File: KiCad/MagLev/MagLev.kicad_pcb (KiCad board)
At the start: 2 copper layers, 79 parts, among them J1 Barrel_Jack, Q1 ZX5T851GTA, Q2 ZX5T1951GTA, Q3 ZX5T851GTA, Q4 ZX5T1951GTA, Q5 ZX5T1951GTA, Q6 ZX5T851GTA, Q7 ZX5T1951GTA, Q8 ZX5T851GTA, Q9 ZX5T1951GTA, U1 LM324, U10 DRV5505, U11 DRV5505, U12 DRV5505, U2 LM324, U3 L78L05_SO8, U4 TL431A, U5 LM393

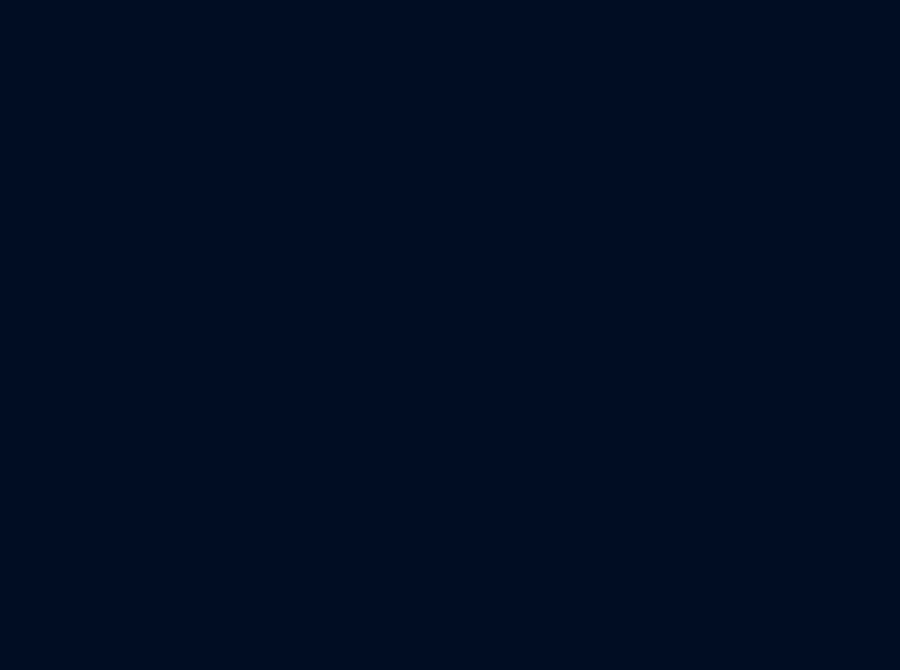
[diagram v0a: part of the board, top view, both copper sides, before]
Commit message: Update spice model to match enbs design. Add TVS diodes to schematic.
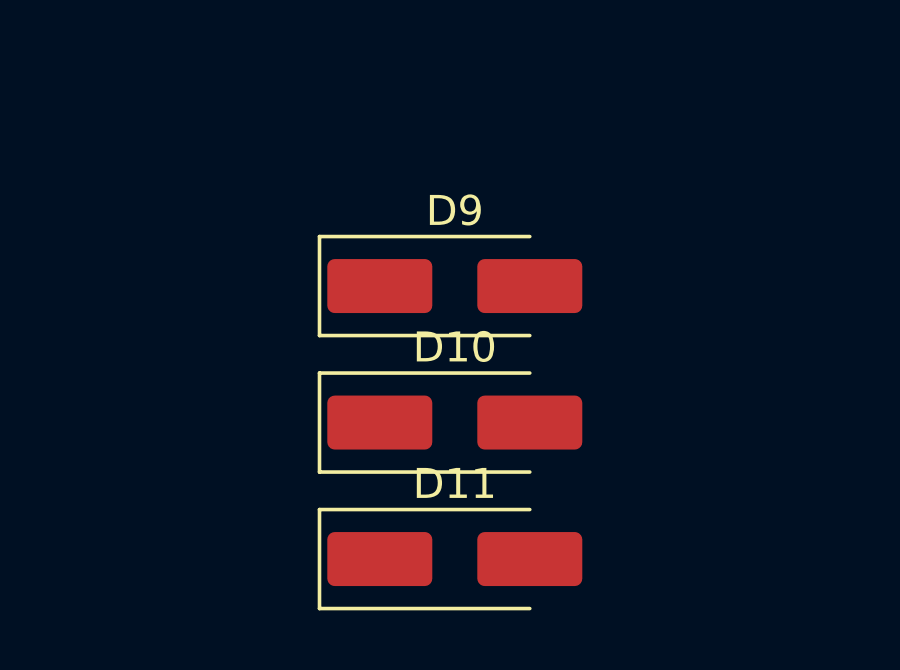
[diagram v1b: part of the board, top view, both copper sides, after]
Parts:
- added D10: SMAJ12A, Diode_SMD:D_SMA_Handsoldering, F.Cu at (-38.1, 145.3)
- added D11: SMAJ12A, Diode_SMD:D_SMA_Handsoldering, F.Cu at (-38.1, 149.9)
- added D9: SMAJ5.0A, Diode_SMD:D_SMA_Handsoldering, F.Cu at (-38.1, 140.8)
- renumbered L1 to X1, L2 to X2, L3 to Y1, L4 to Y2

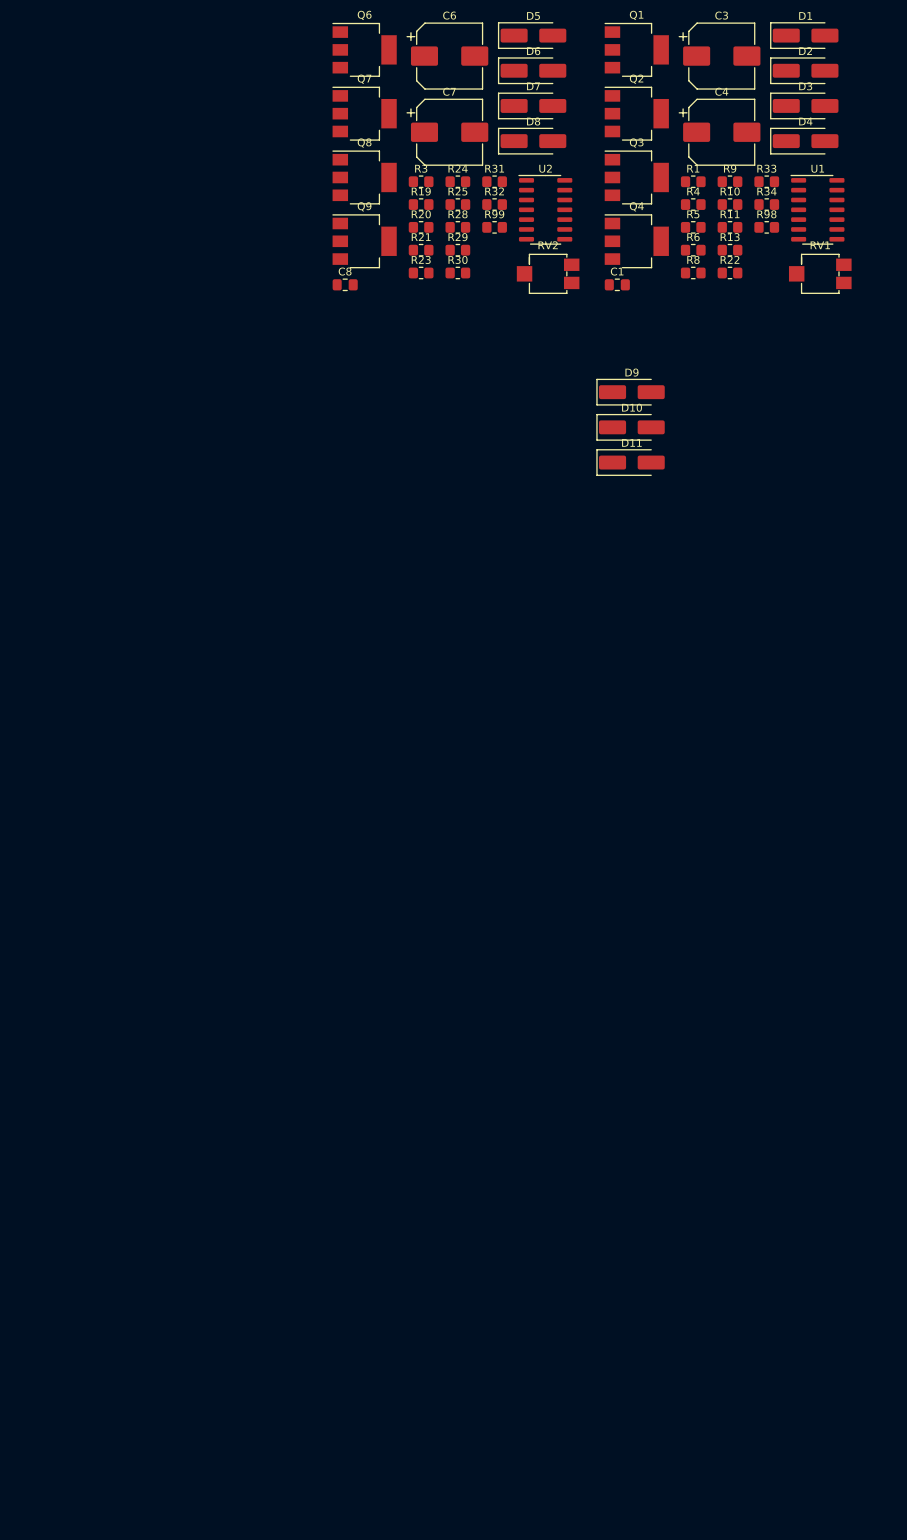
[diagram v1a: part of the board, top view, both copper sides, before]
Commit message: Assign footprints to MCU components.
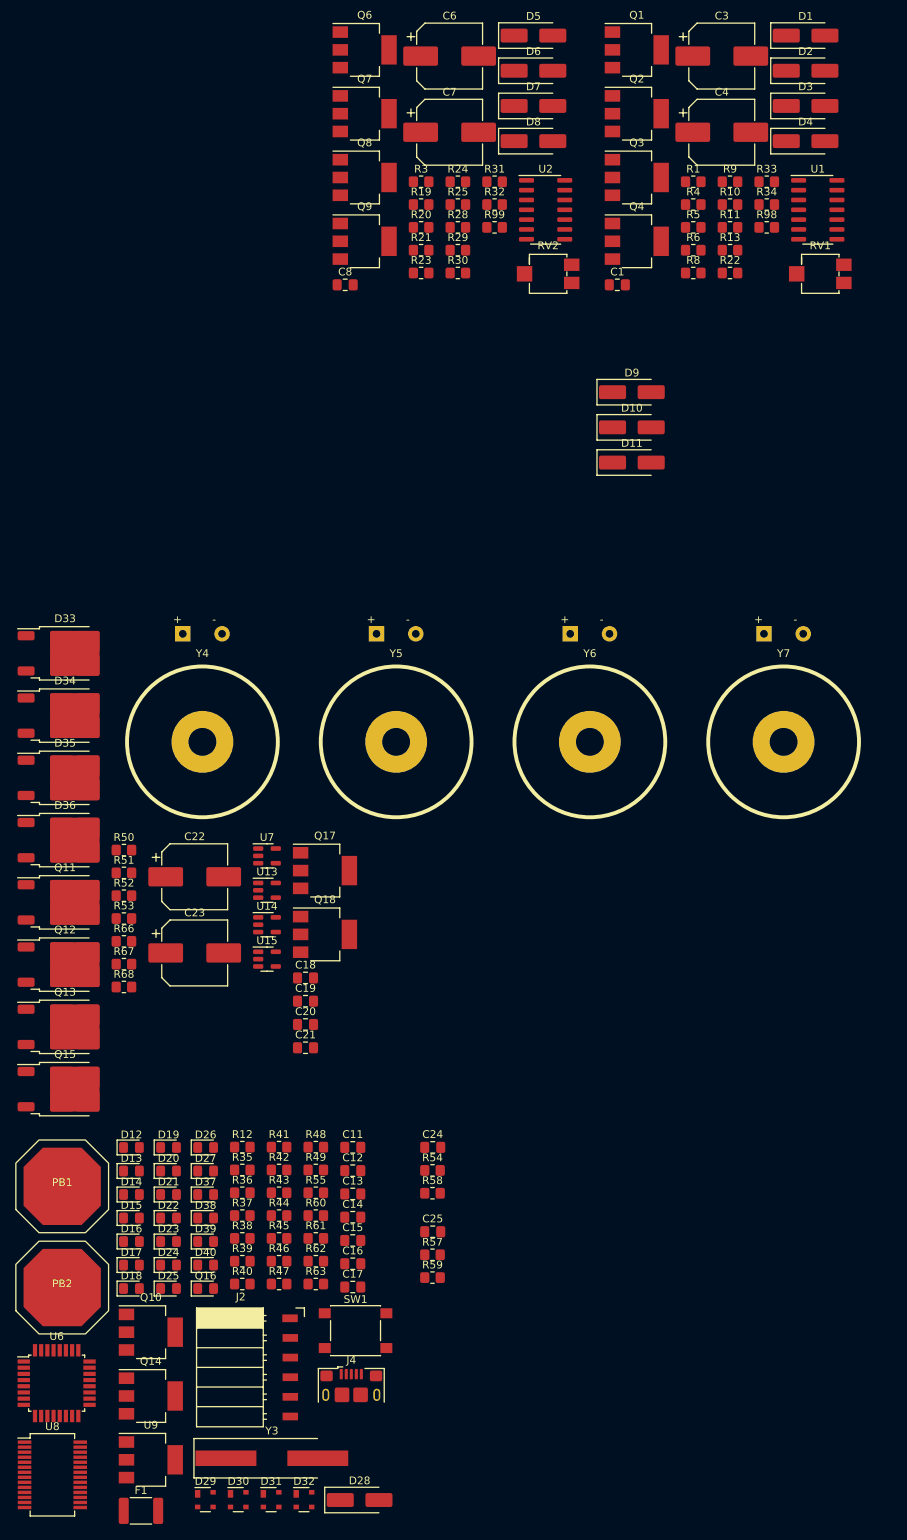
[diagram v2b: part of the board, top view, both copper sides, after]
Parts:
- added C11: 22pF, Capacitor_SMD:C_0805_2012Metric_Pad1.18x1.45mm_HandSolder, F.Cu at (-74.2, 238.4)
- added C12: 22pF, Capacitor_SMD:C_0805_2012Metric_Pad1.18x1.45mm_HandSolder, F.Cu at (-74.2, 241.4)
- added C13: 0.1uF, Capacitor_SMD:C_0805_2012Metric_Pad1.18x1.45mm_HandSolder, F.Cu at (-74.2, 244.4)
- added C14: 100nF, Capacitor_SMD:C_0805_2012Metric_Pad1.18x1.45mm_HandSolder, F.Cu at (-74.2, 247.4)
- added C15: 100nF, Capacitor_SMD:C_0805_2012Metric_Pad1.18x1.45mm_HandSolder, F.Cu at (-74.2, 250.5)
- added C16: 10uF, Capacitor_SMD:C_0805_2012Metric_Pad1.18x1.45mm_HandSolder, F.Cu at (-74.2, 253.5)
- added C17: 10uF, Capacitor_SMD:C_0805_2012Metric_Pad1.18x1.45mm_HandSolder, F.Cu at (-74.2, 256.5)
- added C18: 0.1uF, Capacitor_SMD:C_0805_2012Metric_Pad1.18x1.45mm_HandSolder, F.Cu at (-80.3, 216.5)
- added C19: 0.1uF, Capacitor_SMD:C_0805_2012Metric_Pad1.18x1.45mm_HandSolder, F.Cu at (-80.3, 219.5)
- added C20: 0.1uF, Capacitor_SMD:C_0805_2012Metric_Pad1.18x1.45mm_HandSolder, F.Cu at (-80.3, 222.5)
- added C21: 0.1uF, Capacitor_SMD:C_0805_2012Metric_Pad1.18x1.45mm_HandSolder, F.Cu at (-80.3, 225.5)
- added C22: 220uF, Maglev_Footprint_Library:CP_Elec_8x10_HandSolder, F.Cu at (-94.6, 203.4)
- added C23: 220uF, Maglev_Footprint_Library:CP_Elec_8x10_HandSolder, F.Cu at (-94.6, 213.3)
- added C24: 0.4n, Capacitor_SMD:C_0805_2012Metric_Pad1.18x1.45mm_HandSolder, F.Cu at (-63.8, 238.4)
- added C25: 0.4n, Capacitor_SMD:C_0805_2012Metric_Pad1.18x1.45mm_HandSolder, F.Cu at (-63.8, 249.3)
- added D12: LED, LED_SMD:LED_0805_2012Metric_Pad1.15x1.40mm_HandSolder, F.Cu at (-102.8, 238.4)
- added D13: LED, LED_SMD:LED_0805_2012Metric_Pad1.15x1.40mm_HandSolder, F.Cu at (-102.8, 241.5)
- added D14: LED, LED_SMD:LED_0805_2012Metric_Pad1.15x1.40mm_HandSolder, F.Cu at (-102.8, 244.5)
- added D15: LED, LED_SMD:LED_0805_2012Metric_Pad1.15x1.40mm_HandSolder, F.Cu at (-102.8, 247.5)
- added D16: LED, LED_SMD:LED_0805_2012Metric_Pad1.15x1.40mm_HandSolder, F.Cu at (-102.8, 250.6)
- added D17: LED, LED_SMD:LED_0805_2012Metric_Pad1.15x1.40mm_HandSolder, F.Cu at (-102.8, 253.6)
- added D18: LED, LED_SMD:LED_0805_2012Metric_Pad1.15x1.40mm_HandSolder, F.Cu at (-102.8, 256.7)
- added D19: LED, LED_SMD:LED_0805_2012Metric_Pad1.15x1.40mm_HandSolder, F.Cu at (-98.0, 238.4)
- added D20: LED, LED_SMD:LED_0805_2012Metric_Pad1.15x1.40mm_HandSolder, F.Cu at (-98.0, 241.5)
- added D21: LED, LED_SMD:LED_0805_2012Metric_Pad1.15x1.40mm_HandSolder, F.Cu at (-98.0, 244.5)
- added D22: LED, LED_SMD:LED_0805_2012Metric_Pad1.15x1.40mm_HandSolder, F.Cu at (-98.0, 247.5)
- added D23: LED, LED_SMD:LED_0805_2012Metric_Pad1.15x1.40mm_HandSolder, F.Cu at (-98.0, 250.6)
- added D24: LED, LED_SMD:LED_0805_2012Metric_Pad1.15x1.40mm_HandSolder, F.Cu at (-98.0, 253.6)
- added D25: LED, LED_SMD:LED_0805_2012Metric_Pad1.15x1.40mm_HandSolder, F.Cu at (-98.0, 256.7)
- added D26: LED, LED_SMD:LED_0805_2012Metric_Pad1.15x1.40mm_HandSolder, F.Cu at (-93.2, 238.4)
- added D27: LED, LED_SMD:LED_0805_2012Metric_Pad1.15x1.40mm_HandSolder, F.Cu at (-93.2, 241.5)
- added D28: D, Diode_SMD:D_SMA_Handsoldering, F.Cu at (-73.3, 284.0)
- added D29: SP0503BAHT, Package_TO_SOT_SMD:SOT-143, F.Cu at (-93.2, 284.0)
- added D30: SP0503BAHT, Package_TO_SOT_SMD:SOT-143, F.Cu at (-89.0, 284.0)
- added D31: SP0503BAHT, Package_TO_SOT_SMD:SOT-143, F.Cu at (-84.7, 284.0)
- added D32: SP0503BAHT, Package_TO_SOT_SMD:SOT-143, F.Cu at (-80.5, 284.0)
- added D33: D, Maglev_Footprint_Library:TO-252-Schottkey, F.Cu at (-111.4, 174.5)
- added D34: D, Maglev_Footprint_Library:TO-252-Schottkey, F.Cu at (-111.4, 182.6)
- added D35: D, Maglev_Footprint_Library:TO-252-Schottkey, F.Cu at (-111.4, 190.6)
- added D36: D, Maglev_Footprint_Library:TO-252-Schottkey, F.Cu at (-111.4, 198.7)
- added D37: Blue, LED_SMD:LED_0805_2012Metric_Pad1.15x1.40mm_HandSolder, F.Cu at (-93.2, 244.5)
- added D38: Blue, LED_SMD:LED_0805_2012Metric_Pad1.15x1.40mm_HandSolder, F.Cu at (-93.2, 247.5)
- added D39: Green, LED_SMD:LED_0805_2012Metric_Pad1.15x1.40mm_HandSolder, F.Cu at (-93.2, 250.6)
- added D40: Red, LED_SMD:LED_0805_2012Metric_Pad1.15x1.40mm_HandSolder, F.Cu at (-93.2, 253.6)
- added F1: MF-MSMF050-2, Fuse:Fuse_1812_4532Metric_Pad1.30x3.40mm_HandSolder, F.Cu at (-101.6, 285.4)
- added J2: Programming header, Maglev_Footprint_Library:PinSocket_1x06_P2.54mm_Horizontal_SM, F.Cu at (-84.3, 260.5)
- added J4: USB_B_Micro, Connector_USB:USB_Micro-B_Amphenol_10118193-0001LF_Horizontal, F.Cu at (-74.4, 270.4)
- added PB1: ~, Maglev_Footprint_Library:Capacitive_Touch_Pad, F.Cu at (-111.8, 243.5)
- added PB2: ~, Maglev_Footprint_Library:Capacitive_Touch_Pad, F.Cu at (-111.8, 256.5)
- added Q10: ZX5T851GTA, Maglev_Footprint_Library:SOT-223-3_TabPin2_BJT, F.Cu at (-100.3, 262.3)
- added Q11: AOD442G, Package_TO_SOT_SMD:TO-252-2, F.Cu at (-111.4, 206.7)
- added Q12: AOD442G, Package_TO_SOT_SMD:TO-252-2, F.Cu at (-111.4, 214.8)
- added Q13: AOD442G, Package_TO_SOT_SMD:TO-252-2, F.Cu at (-111.4, 222.8)
- added Q14: ZX5T851GTA, Maglev_Footprint_Library:SOT-223-3_TabPin2_BJT, F.Cu at (-100.3, 270.6)
- added Q15: AOD442G, Package_TO_SOT_SMD:TO-252-2, F.Cu at (-111.4, 230.9)
- added Q16: TEMT7000X01, LED_SMD:LED_0805_2012Metric_Pad1.15x1.40mm_HandSolder, F.Cu at (-93.2, 256.7)
- added Q17: ZX5T851GTA, Maglev_Footprint_Library:SOT-223-3_TabPin2_BJT, F.Cu at (-77.8, 202.6)
- added Q18: ZX5T1951GTA, Maglev_Footprint_Library:SOT-223-3_TabPin2_BJT, F.Cu at (-77.8, 210.9)
- added R12: 1k, Resistor_SMD:R_0805_2012Metric_Pad1.20x1.40mm_HandSolder, F.Cu at (-88.5, 238.4)
- added R35: 1k, Resistor_SMD:R_0805_2012Metric_Pad1.20x1.40mm_HandSolder, F.Cu at (-88.5, 241.3)
- added R36: 1k, Resistor_SMD:R_0805_2012Metric_Pad1.20x1.40mm_HandSolder, F.Cu at (-88.5, 244.3)
- added R37: 1k, Resistor_SMD:R_0805_2012Metric_Pad1.20x1.40mm_HandSolder, F.Cu at (-88.5, 247.2)
- added R38: 1k, Resistor_SMD:R_0805_2012Metric_Pad1.20x1.40mm_HandSolder, F.Cu at (-88.5, 250.2)
- added R39: 1k, Resistor_SMD:R_0805_2012Metric_Pad1.20x1.40mm_HandSolder, F.Cu at (-88.5, 253.1)
- added R40: 1MEG, Resistor_SMD:R_0805_2012Metric_Pad1.20x1.40mm_HandSolder, F.Cu at (-88.5, 256.1)
- added R41: 1k, Resistor_SMD:R_0805_2012Metric_Pad1.20x1.40mm_HandSolder, F.Cu at (-83.7, 238.4)
- added R42: 1k, Resistor_SMD:R_0805_2012Metric_Pad1.20x1.40mm_HandSolder, F.Cu at (-83.7, 241.3)
- added R43: 1k, Resistor_SMD:R_0805_2012Metric_Pad1.20x1.40mm_HandSolder, F.Cu at (-83.7, 244.3)
- added R44: 1k, Resistor_SMD:R_0805_2012Metric_Pad1.20x1.40mm_HandSolder, F.Cu at (-83.7, 247.2)
- added R45: 1k, Resistor_SMD:R_0805_2012Metric_Pad1.20x1.40mm_HandSolder, F.Cu at (-83.7, 250.2)
- added R46: 1k, Resistor_SMD:R_0805_2012Metric_Pad1.20x1.40mm_HandSolder, F.Cu at (-83.7, 253.1)
- added R47: 1k, Resistor_SMD:R_0805_2012Metric_Pad1.20x1.40mm_HandSolder, F.Cu at (-83.7, 256.1)
- added R48: 1M, Resistor_SMD:R_0805_2012Metric_Pad1.20x1.40mm_HandSolder, F.Cu at (-79.0, 238.4)
- added R49: 1M, Resistor_SMD:R_0805_2012Metric_Pad1.20x1.40mm_HandSolder, F.Cu at (-79.0, 241.3)
- added R50: 1k, Resistor_SMD:R_0805_2012Metric_Pad1.20x1.40mm_HandSolder, F.Cu at (-103.8, 200.0)
- added R51: 1k, Resistor_SMD:R_0805_2012Metric_Pad1.20x1.40mm_HandSolder, F.Cu at (-103.8, 202.9)
- added R52: 1k, Resistor_SMD:R_0805_2012Metric_Pad1.20x1.40mm_HandSolder, F.Cu at (-103.8, 205.9)
- added R53: 1k, Resistor_SMD:R_0805_2012Metric_Pad1.20x1.40mm_HandSolder, F.Cu at (-103.8, 208.8)
- added R54: 1k, Resistor_SMD:R_0805_2012Metric_Pad1.20x1.40mm_HandSolder, F.Cu at (-63.9, 241.4)
- added R55: 5k, Resistor_SMD:R_0805_2012Metric_Pad1.20x1.40mm_HandSolder, F.Cu at (-79.0, 244.3)
- added R57: 1k, Resistor_SMD:R_0805_2012Metric_Pad1.20x1.40mm_HandSolder, F.Cu at (-63.9, 252.3)
- added R58: 1k, Resistor_SMD:R_0805_2012Metric_Pad1.20x1.40mm_HandSolder, F.Cu at (-63.9, 244.3)
- added R59: 1k, Resistor_SMD:R_0805_2012Metric_Pad1.20x1.40mm_HandSolder, F.Cu at (-63.9, 255.3)
- added R60: 1k, Resistor_SMD:R_0805_2012Metric_Pad1.20x1.40mm_HandSolder, F.Cu at (-79.0, 247.2)
- added R61: 1k, Resistor_SMD:R_0805_2012Metric_Pad1.20x1.40mm_HandSolder, F.Cu at (-79.0, 250.2)
- added R62: 1k, Resistor_SMD:R_0805_2012Metric_Pad1.20x1.40mm_HandSolder, F.Cu at (-79.0, 253.1)
- added R63: 1k, Resistor_SMD:R_0805_2012Metric_Pad1.20x1.40mm_HandSolder, F.Cu at (-79.0, 256.1)
- added R66: 1k, Resistor_SMD:R_0805_2012Metric_Pad1.20x1.40mm_HandSolder, F.Cu at (-103.8, 211.8)
- added R67: 10k, Resistor_SMD:R_0805_2012Metric_Pad1.20x1.40mm_HandSolder, F.Cu at (-103.8, 214.7)
- added R68: 0, Resistor_SMD:R_0805_2012Metric_Pad1.20x1.40mm_HandSolder, F.Cu at (-103.8, 217.7)
- added SW1: PTS645, Button_Switch_SMD:SW_SPST_PTS645, F.Cu at (-73.8, 262.1)
- added U13: MCP1402, Package_TO_SOT_SMD:SOT-23-5, F.Cu at (-85.3, 205.2)
- added U14: MCP1402, Package_TO_SOT_SMD:SOT-23-5, F.Cu at (-85.3, 209.6)
- added U15: MCP1402, Package_TO_SOT_SMD:SOT-23-5, F.Cu at (-85.3, 214.1)
- added U6: ATmega328P-A, Package_QFP:TQFP-32_7x7mm_P0.8mm, F.Cu at (-112.5, 268.9)
- added U7: MCP1402, Package_TO_SOT_SMD:SOT-23-5, F.Cu at (-85.3, 200.7)
- added U8: FT232RL, Package_SO:SSOP-28_5.3x10.2mm_P0.65mm, F.Cu at (-113.0, 280.8)
- added U9: LM1117MP-5.0, Package_TO_SOT_SMD:SOT-223-3_TabPin2, F.Cu at (-100.3, 278.8)
- added Y3: J49SMH-16MHz, Crystal:Crystal_SMD_HC49-SD_HandSoldering, F.Cu at (-84.6, 278.6)
- added Y4: L_Ferrite, Maglev_Footprint_Library:Maglev_coil, F.Cu at (-93.6, 186.0)
- added Y5: L_Ferrite, Maglev_Footprint_Library:Maglev_coil, F.Cu at (-68.6, 186.0)
- added Y6: L_Ferrite, Maglev_Footprint_Library:Maglev_coil, F.Cu at (-43.5, 186.0)
- added Y7: L_Ferrite, Maglev_Footprint_Library:Maglev_coil, F.Cu at (-18.5, 186.0)
- C3, C4, C6, C7: footprint Capacitor_SMD:CP_Elec_8x10 -> Maglev_Footprint_Library:CP_Elec_8x10_HandSolder
- RV1, RV2: value 1k -> 10k
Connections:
- C9 pad 1: /Vcc -> /Vcc_en
- D10 pad 1: /Vcc -> VCC
- D2 pad 2: GND1 -> GND
- D4 pad 2: GND1 -> GND
- D6 pad 2: GND1 -> GND
- D8 pad 2: GND1 -> GND
- D9 pad 2: GND1 -> GND
- J1 pad 1: /Vcc -> VCC
- Q2 pad 1: GND1 -> GND
- Q4 pad 1: GND1 -> GND
- Q5 pad 3: /Vcc -> /Vcc_en
- Q7 pad 1: GND1 -> GND
- Q9 pad 1: GND1 -> GND
- R15 pad 1: /Vcc -> VCC
- U3 pad 3: /Vcc -> /Vcc_en
- U5 pad 8: /Vcc -> /Vcc_en

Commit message: Add netclasses, define PCB rules.
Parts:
- removed C18, C21: 0.1uF, Capacitor_SMD:C_0805_2012Metric_Pad1.18x1.45mm_HandSolder
- removed D33, D36: D, Maglev_Footprint_Library:TO-252-Schottkey
- removed Q11, Q15: AOD442G, Package_TO_SOT_SMD:TO-252-2
- removed R50, R52, R53: 1k, Resistor_SMD:R_0805_2012Metric_Pad1.20x1.40mm_HandSolder
- removed U15, U7: MCP1402, Package_TO_SOT_SMD:SOT-23-5
- removed Y4, Y7: L_Ferrite, Maglev_Footprint_Library:Maglev_coil
- added TP1: CoilPWM, TestPoint:TestPoint_Pad_D2.0mm, F.Cu at (-82.3, 49.1)
- added TP10: DR, TestPoint:TestPoint_Pad_D2.0mm, F.Cu at (-78.3, 65.3)
- added TP11: Gc, TestPoint:TestPoint_Pad_D2.0mm, F.Cu at (-48.5, 71.9)
- added TP12: Gc, TestPoint:TestPoint_Pad_D2.0mm, F.Cu at (-48.5, 112.9)
- added TP13: Gx, TestPoint:TestPoint_Pad_D2.0mm, F.Cu at (-48.5, 75.9)
- added TP14: Gx, TestPoint:TestPoint_Pad_D2.0mm, F.Cu at (-48.5, 116.9)
- added TP15: Gy, TestPoint:TestPoint_Pad_D2.0mm, F.Cu at (-48.5, 80.0)
- added TP16: Gy, TestPoint:TestPoint_Pad_D2.0mm, F.Cu at (-48.5, 121.0)
- added TP17: LS, TestPoint:TestPoint_Pad_D2.0mm, F.Cu at (-11.8, 16.9)
- added TP18: UV, TestPoint:TestPoint_Pad_D2.0mm, F.Cu at (-11.8, 20.9)
- added TP19: WH, TestPoint:TestPoint_Pad_D2.0mm, F.Cu at (-11.8, 25.0)
- added TP2: Vreg, TestPoint:TestPoint_Pad_D2.0mm, F.Cu at (-82.3, 53.1)
- added TP20: Yin, TestPoint:TestPoint_Pad_D2.0mm, F.Cu at (-48.5, 84.0)
- added TP21: Yin, TestPoint:TestPoint_Pad_D2.0mm, F.Cu at (-48.5, 125.0)
- added TP22: Xin, TestPoint:TestPoint_Pad_D2.0mm, F.Cu at (-48.5, 88.1)
- added TP23: Xin, TestPoint:TestPoint_Pad_D2.0mm, F.Cu at (-48.5, 129.1)
- added TP3: Vref+, TestPoint:TestPoint_Pad_D2.0mm, F.Cu at (-82.3, 57.2)
- added TP4: Vref-, TestPoint:TestPoint_Pad_D2.0mm, F.Cu at (-82.3, 61.2)
- added TP5: En_sig, TestPoint:TestPoint_Pad_D2.0mm, F.Cu at (-82.3, 65.3)
- added TP6: Vb_Zaxis, TestPoint:TestPoint_Pad_D2.0mm, F.Cu at (-78.3, 49.1)
- added TP7: Hx, TestPoint:TestPoint_Pad_D2.0mm, F.Cu at (-78.3, 53.1)
- added TP8: Hy, TestPoint:TestPoint_Pad_D2.0mm, F.Cu at (-78.3, 57.2)
- added TP9: Vcc_en, TestPoint:TestPoint_Pad_D2.0mm, F.Cu at (-78.3, 61.2)
- added Y8: L_Ferrite, Maglev_Footprint_Library:Maglev_coil, B.Cu at (131.4, 80.6)
- added Y9: L_Ferrite, Maglev_Footprint_Library:Maglev_coil, B.Cu at (131.4, 122.6)
- R2: value 1 -> 1k
- U10: value DRV5505 -> X; moved to B.Cu
- U11: value DRV5505 -> Y; moved to B.Cu
- U12: value DRV5505 -> Z; moved to B.Cu
- Y5, Y6: moved to B.Cu
- moved J2 333.6 mm to (155.6, 28.7), turned to -90 degrees
- moved PB1 265.3 mm to (143.3, 170.4)
- moved Y5 250.1 mm to (173.4, 122.6), turned to 90 degrees
- moved F1 249.6 mm to (-17.8, 50.2)
- moved D35 248.5 mm to (111.5, 80.8), turned to 90 degrees
- moved PB2 248.3 mm to (120.9, 169.9)
- moved U6 247.0 mm to (68.1, 100.3)
- moved Q13 243.4 mm to (110.5, 122.7)
- moved Y6 241.2 mm to (173.4, 80.6), turned to 90 degrees
- moved U8 240.8 mm to (-55.1, 47.0)
- moved D18 229.5 mm to (-44.8, 34.6)
- moved D25 229.5 mm to (-40.0, 34.6)
- moved Q16 229.5 mm to (-35.3, 34.6)
- moved C11 229.5 mm to (-16.2, 16.4)
- moved C12 229.5 mm to (-16.2, 19.4)
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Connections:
- R1 pad 1: Net-(U1B--) -> Net-(R1-Pad1)
- R1 pad 2: Net-(R1-Pad2) -> Net-(U1B--)
- R10 pad 2: Net-(R1-Pad2) -> Net-(R1-Pad1)
- R2 pad 1: GND -> /CoilPWM
- R2 pad 2: GND1 -> Net-(U14-IN)
- R28 pad 1: Net-(U2B--) -> Net-(R28-Pad1)
- R28 pad 2: Net-(R28-Pad2) -> Net-(U2B--)
- R29 pad 2: Net-(R28-Pad2) -> Net-(R28-Pad1)
- R30 pad 1: Net-(R28-Pad2) -> Net-(R28-Pad1)
- R33 pad 1: Net-(R1-Pad2) -> Net-(R1-Pad1)
- R51 pad 1: Net-(U13-IN) -> /CoilPWM
- R51 pad 2: /CoilPWM -> Net-(U13-IN)
- Y5 pad 1: VCC -> Net-(Y5-Pad1)
- Y6 pad 2: Net-(D35-A) -> Net-(Y5-Pad1)
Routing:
- net Net-(Y1-Pad2): track 0.00 -> 75.5 mm
- net Net-(X1-Pad2): track 0.00 -> 72.1 mm
- net Net-(Y5-Pad1): track 0.00 -> 53.3 mm
- net Net-(D35-A): track 0.00 -> 44.5 mm
- net Net-(Y8-Pad2): track 0.00 -> 40.5 mm
- net VCC: track 0.00 -> 4.49 mm
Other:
- rule pad_to_mask_clearance: 0 -> 0.038
